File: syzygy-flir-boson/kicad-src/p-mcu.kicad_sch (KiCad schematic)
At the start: 5 parts, among them J3 TagConnect, U2 ATtiny44A-MMH

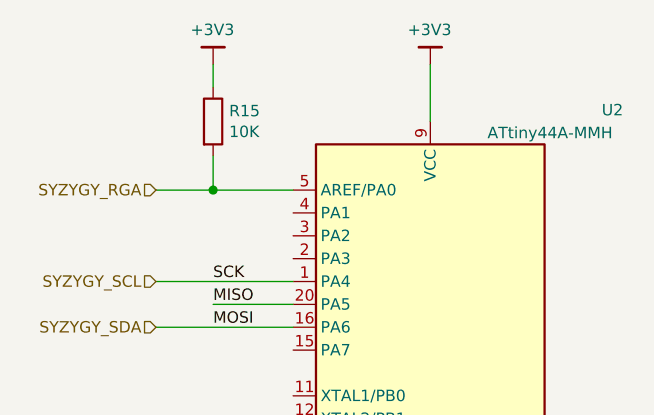
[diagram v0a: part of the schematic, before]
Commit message: syzygy-boson: Add BOM values to project
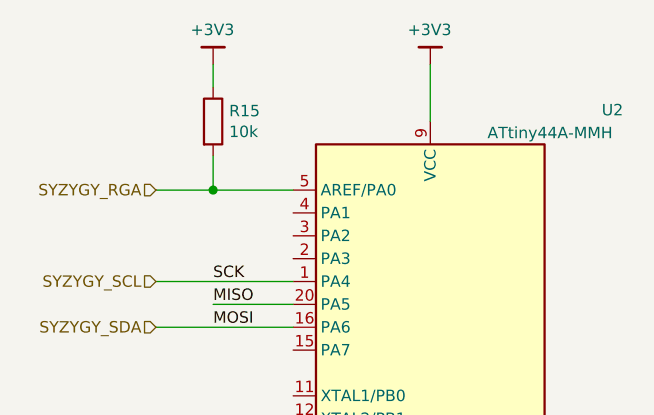
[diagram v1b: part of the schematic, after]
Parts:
- C10: Mfg Samsung Electro-Mechanics -> Yageo; PN CL05A105KP5NNNC -> CC0402KRX5R8BB105
- C9: Mfg Samsung Electro-Mechanics -> Yageo; PN CL05B104KP5NNNC -> CC0402JRX7R7BB104
- R15: value 10K -> 10k; Mfg Stackpole Electronics Inc -> Yageo; PN RMCF0402FT10K0 -> RC0402JR-0710KL
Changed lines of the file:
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@@
-(kicad_sch (version 20201015) (generator eeschema)
+(kicad_sch (version 20210126) (generator eeschema)
   (paper "A4")
   (title_block
@@
       (effects (font (size 1.27 1.27)) hide)
     )
+    (pin "1")
   )
   (symbol (lib_id "gkl_power:GND") (at 194.31 100.33 0) (mirror y) (unit 1)
@@
       (effects (font (size 1.27 1.27)) hide)
     )
+    (pin "1")
   )
   (symbol (lib_id "gkl_power:GND") (at 207.01 100.33 0) (mirror y) (unit 1)
@@
       (effects (font (size 1.27 1.27)) hide)
     )
+    (pin "1")
   )
   (symbol (lib_id "gkl_power:GND") (at 213.36 128.27 0) (mirror y) (unit 1)
@@
       (effects (font (size 1.27 1.27)) hide)
     )
+    (pin "1")
   )
   (symbol (lib_id "gkl_power:+3V3") (at 132.08 68.58 0) (mirror y) (unit 1)
@@
       (effects (font (size 1.27 1.27)) hide)
     )
+    (pin "1")
   )
   (symbol (lib_id "gkl_power:+3V3") (at 156.21 68.58 0) (mirror y) (unit 1)
@@
       (effects (font (size 1.27 1.27)) hide)
     )
+    (pin "1")
   )
   (symbol (lib_id "gkl_power:+3V3") (at 194.31 85.09 0) (mirror y) (unit 1)
@@
       (effects (font (size 1.27 1.27)) hide)
     )
+    (pin "1")
   )
   (symbol (lib_id "gkl_power:+3V3") (at 207.01 85.09 0) (mirror y) (unit 1)
@@
       (effects (font (size 1.27 1.27)) hide)
     )
+    (pin "1")
   )
   (symbol (lib_id "gkl_power:+3V3") (at 213.36 116.84 0) (mirror y) (unit 1)
@@
       (effects (font (size 1.27 1.27)) hide)
     )
+    (pin "1")
   )
   (symbol (lib_id "Device:R") (at 132.08 74.93 0) (unit 1)
@@
       (effects (font (size 1.27 1.27)) (justify left))
     )
-    (property "Value" "10K" (id 1) (at 133.858 76.073 0)
+    (property "Value" "10k" (id 1) (at 133.858 76.073 0)
       (effects (font (size 1.27 1.27)) (justify left))
     )
@@
       (effects (font (size 1.27 1.27)) hide)
     )
-    (property "Datasheet" "~" (id 3) (at 132.08 74.93 0)
-      (effects (font (size 1.27 1.27)) hide)
-    )
-    (property "Mfg" "Stackpole Electronics Inc" (id 4) (at 0 149.86 0)
-      (effects (font (size 1.27 1.27)) hide)
-    )
-    (property "PN" "RMCF0402FT10K0" (id 5) (at 0 149.86 0)
-      (effects (font (size 1.27 1.27)) hide)
-    )
+    (property "Datasheet" "" (id 3) (at 132.08 74.93 0)
+      (effects (font (size 1.27 1.27)) hide)
+    )
+    (property "Mfg" "Yageo" (id 4) (at 0 149.86 0)
+      (effects (font (size 1.27 1.27)) hide)
+    )
+    (property "PN" "RC0402JR-0710KL" (id 5) (at 0 149.86 0)
+      (effects (font (size 1.27 1.27)) hide)
+    )
+    (pin "1")
+    (pin "2")
   )
   (symbol (lib_id "Device:C") (at 194.31 92.71 0) (unit 1)
@@
       (effects (font (size 1.27 1.27)) hide)
     )
-    (property "Datasheet" "~" (id 3) (at 194.31 92.71 0)
-      (effects (font (size 1.27 1.27)) hide)
-    )
-    (property "PN" "CL05B104KP5NNNC" (id 4) (at -1.27 185.42 0)
-      (effects (font (size 1.27 1.27)) hide)
-    )
-    (property "Mfg" "Samsung Electro-Mechanics" (id 5) (at -1.27 185.42 0)
-      (effects (font (size 1.27 1.27)) hide)
-    )
+    (property "Datasheet" "" (id 3) (at 194.31 92.71 0)
+      (effects (font (size 1.27 1.27)) hide)
+    )
+    (property "PN" "CC0402JRX7R7BB104" (id 4) (at -1.27 185.42 0)
+      (effects (font (size 1.27 1.27)) hide)
+    )
+    (property "Mfg" "Yageo" (id 5) (at -1.27 185.42 0)
+      (effects (font (size 1.27 1.27)) hide)
+    )
+    (pin "1")
+    (pin "2")
   )
   (symbol (lib_id "Device:C") (at 207.01 92.71 0) (unit 1)
@@
       (effects (font (size 1.27 1.27)) hide)
     )
-    (property "Datasheet" "~" (id 3) (at 207.01 92.71 0)
-      (effects (font (size 1.27 1.27)) hide)
-    )
-    (property "PN" "CL05A105KP5NNNC" (id 4) (at 0 185.42 0)
-      (effects (font (size 1.27 1.27)) hide)
-    )
-    (property "Mfg" "Samsung Electro-Mechanics" (id 5) (at 0 185.42 0)
-      (effects (font (size 1.27 1.27)) hide)
-    )
+    (property "Datasheet" "" (id 3) (at 207.01 92.71 0)
+      (effects (font (size 1.27 1.27)) hide)
+    )
+    (property "PN" "CC0402KRX5R8BB105" (id 4) (at 0 185.42 0)
+      (effects (font (size 1.27 1.27)) hide)
+    )
+    (property "Mfg" "Yageo" (id 5) (at 0 185.42 0)
+      (effects (font (size 1.27 1.27)) hide)
+    )
+    (pin "1")
+    (pin "2")
   )
   (symbol (lib_id "Connector_Generic:Conn_02x03_Odd_Even") (at 201.93 123.19 0) (unit 1)
@@
       (effects (font (size 1.27 1.27)) hide)
     )
-    (property "Datasheet" "~" (id 3) (at 201.93 123.19 0)
-      (effects (font (size 1.27 1.27)) hide)
-    )
+    (property "Datasheet" "" (id 3) (at 201.93 123.19 0)
+      (effects (font (size 1.27 1.27)) hide)
+    )
+    (pin "1")
+    (pin "2")
+    (pin "3")
+    (pin "4")
+    (pin "5")
+    (pin "6")
   )
   (symbol (lib_id "SyzygyLVDSPod-rescue:ATtiny44A-MMH-MCU_Microchip_ATtiny") (at 156.21 97.79 0) (mirror y) (unit 1)
@@
       (effects (font (size 1.27 1.27) italic) hide)
     )
-    (property "Datasheet" "http://ww1.microchip.com/downloads/en/DeviceDoc/doc8183.pdf" (id 3) (at 156.21 97.79 0)
+    (property "Datasheet" "" (id 3) (at 156.21 97.79 0)
       (effects (font (size 1.27 1.27)) hide)
     )
@@
       (effects (font (size 1.27 1.27)) hide)
     )
+    (pin "1")
+    (pin "10")
+    (pin "11")
+    (pin "12")
+    (pin "13")
+    (pin "14")
+    (pin "15")
+    (pin "16")
+    (pin "17")
+    (pin "18")
+    (pin "19")
+    (pin "2")
+    (pin "20")
+    (pin "21")
+    (pin "3")
+    (pin "4")
+    (pin "5")
+    (pin "6")
+    (pin "7")
+    (pin "8")
+    (pin "9")
   )
 )
